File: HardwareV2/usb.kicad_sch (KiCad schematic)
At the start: 3 parts

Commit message: commiting before flight :), added in crystal and started doing the labels for the RP2350b
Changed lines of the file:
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@@
 	)
 	(global_label "USB_D-"
-		(shape input)
+		(shape bidirectional)
 		(at 120.65 81.28 0)
 		(fields_autoplaced yes)
@@
 		)
 		(property "Intersheetrefs" "${INTERSHEET_REFS}"
-			(at 131.2552 81.28 0)
+			(at 132.3665 81.28 0)
 			(effects
 				(font
@@
 	)
 	(global_label "USB_D+"
-		(shape input)
+		(shape bidirectional)
 		(at 120.65 86.36 0)
 		(fields_autoplaced yes)
@@
 		)
 		(property "Intersheetrefs" "${INTERSHEET_REFS}"
-			(at 131.2552 86.36 0)
+			(at 132.3665 86.36 0)
 			(effects
 				(font

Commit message: updates pre routing
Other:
- note added: "USB Connector"
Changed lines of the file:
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@@
 	(generator_version "9.0")
 	(paper "A4")
+	(text "USB Connector"
+		(exclude_from_sim no)
+		(at 100.33 47.752 0)
+		(effects
+			(font
+				(size 1.27 1.27)
+			)
+		)
+	)
 	(junction
 		(at 111.76 71.12)

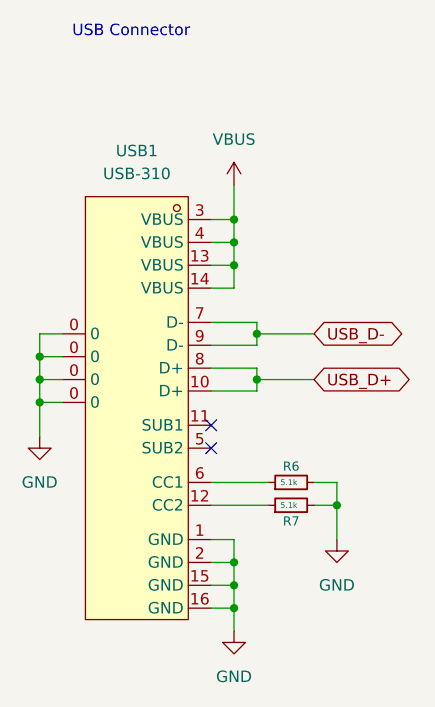
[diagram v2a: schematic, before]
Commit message: initial v2 pcb layout minus passives
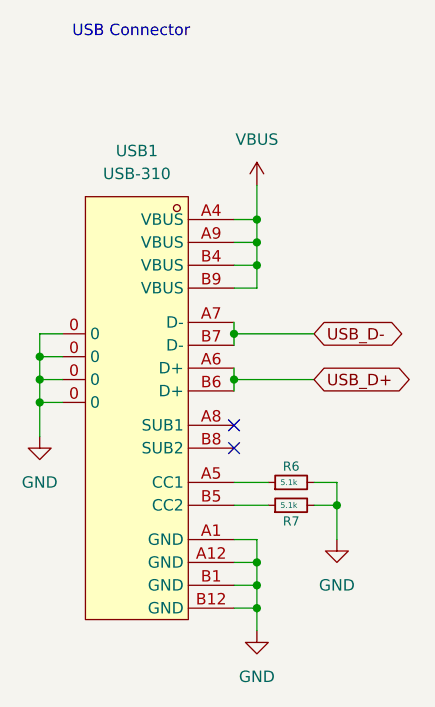
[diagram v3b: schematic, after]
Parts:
- R6, R7: footprint (none) -> Resistor_SMD:R_0805_2012Metric
- USB1: footprint parts_lib:USB-C-SMD_20P-P0.50-L7.4-W8.9 -> RP2350b_parts_layout:USB-C-SMD_20P-P0.50-L7.4-W8.9
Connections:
- net GND: now also USB1.A1 (GND), USB1.A12 (GND), USB1.B1 (GND), USB1.B12 (GND); no longer USB1.1 (GND), USB1.15 (GND), USB1.16 (GND), USB1.2 (GND)
- net USB_D+: now also USB1.A6 (D+), USB1.B6 (D+); no longer USB1.10 (D+), USB1.8 (D+)
- net USB_D-: now also USB1.A7 (D-), USB1.B7 (D-); no longer USB1.7 (D-), USB1.9 (D-)
- net VBUS: now also USB1.A4 (VBUS), USB1.A9 (VBUS), USB1.B4 (VBUS), USB1.B9 (VBUS); no longer USB1.13 (VBUS), USB1.14 (VBUS), USB1.3 (VBUS), USB1.4 (VBUS)
- net at R7.1: now also USB1.B5 (CC2); no longer USB1.12 (CC2)
- net at R6.1: now also USB1.A5 (CC1); no longer USB1.6 (CC1)
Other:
- moved on the sheet: USB1
